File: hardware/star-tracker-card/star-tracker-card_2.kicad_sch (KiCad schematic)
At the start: 94 parts, among them Q2 PMV45EN, Q3 DMP2240UDM, Q4 PMV45EN, Q5 DMP3050LVT-7, Q6 DMP3050LVT-7, U12 MIC842LYC5, U13 MIC842LYC5, U14 MAX4211FETE, U15 TPS62112, U16 MAX7310ATE, U2 TS5A21366DCUR

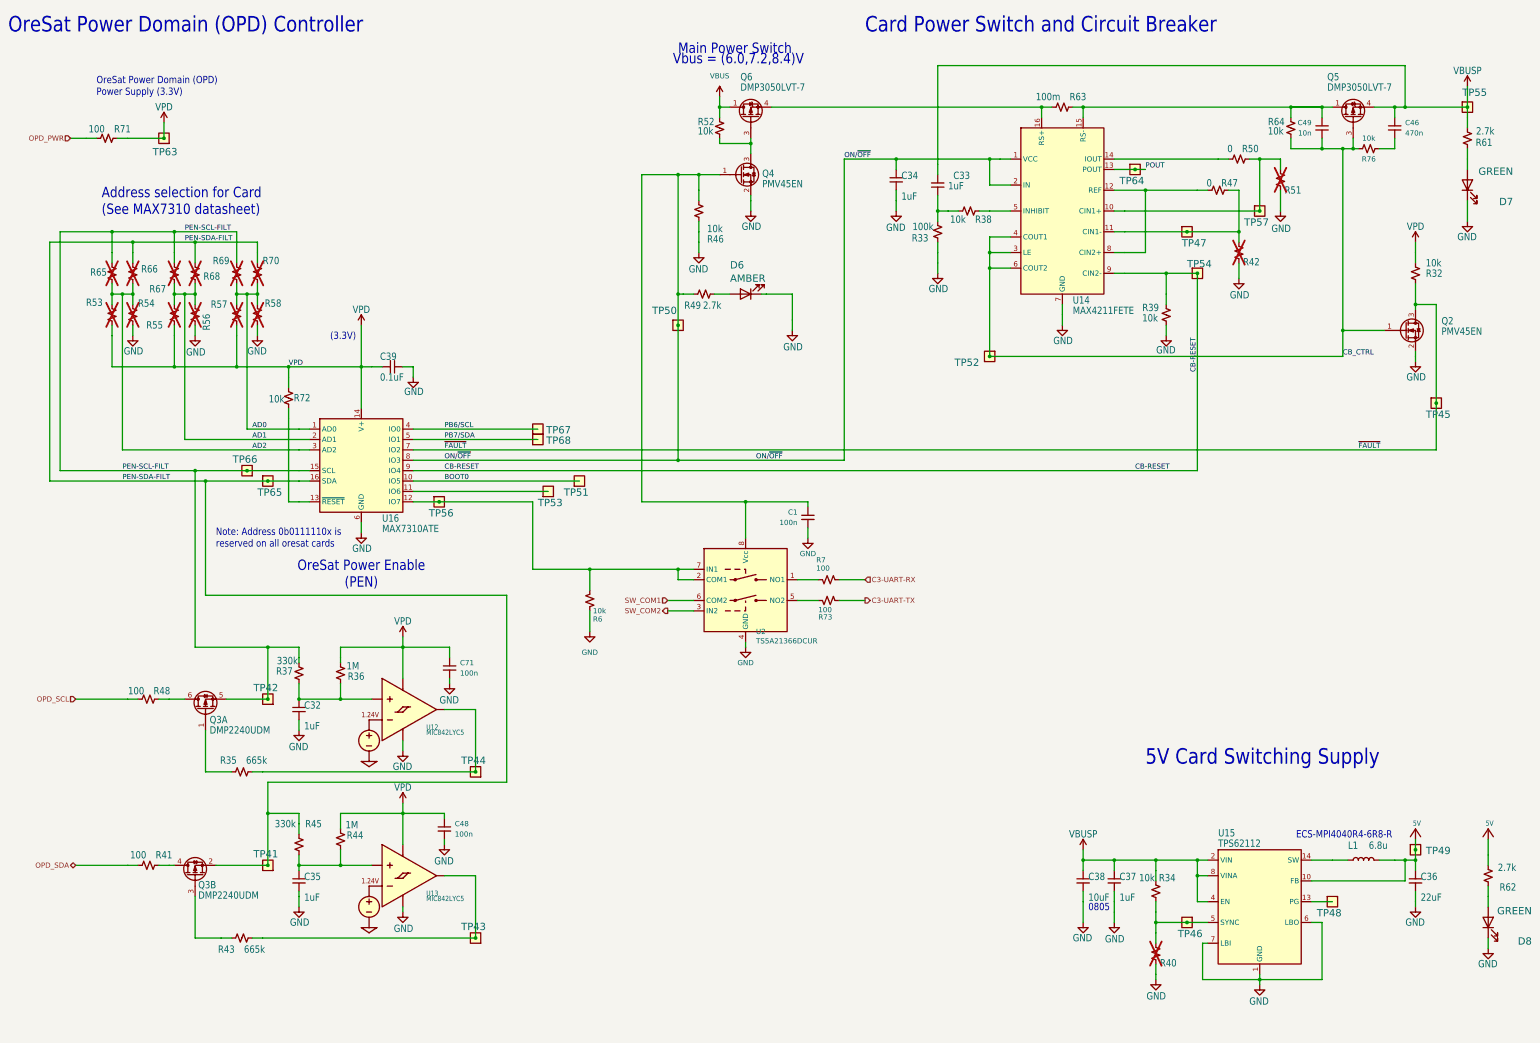
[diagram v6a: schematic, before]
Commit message: Big almost-done cleanup
Fixed a bunch of things in the schematic. Compared against C3 Octavo. Fixed all weird ERCs. Cleaned up a lot of planes on the layout. Moved uart switch, rerouted a bunch of traces for better layout. Fixed library issues, and board/sch sync issues.
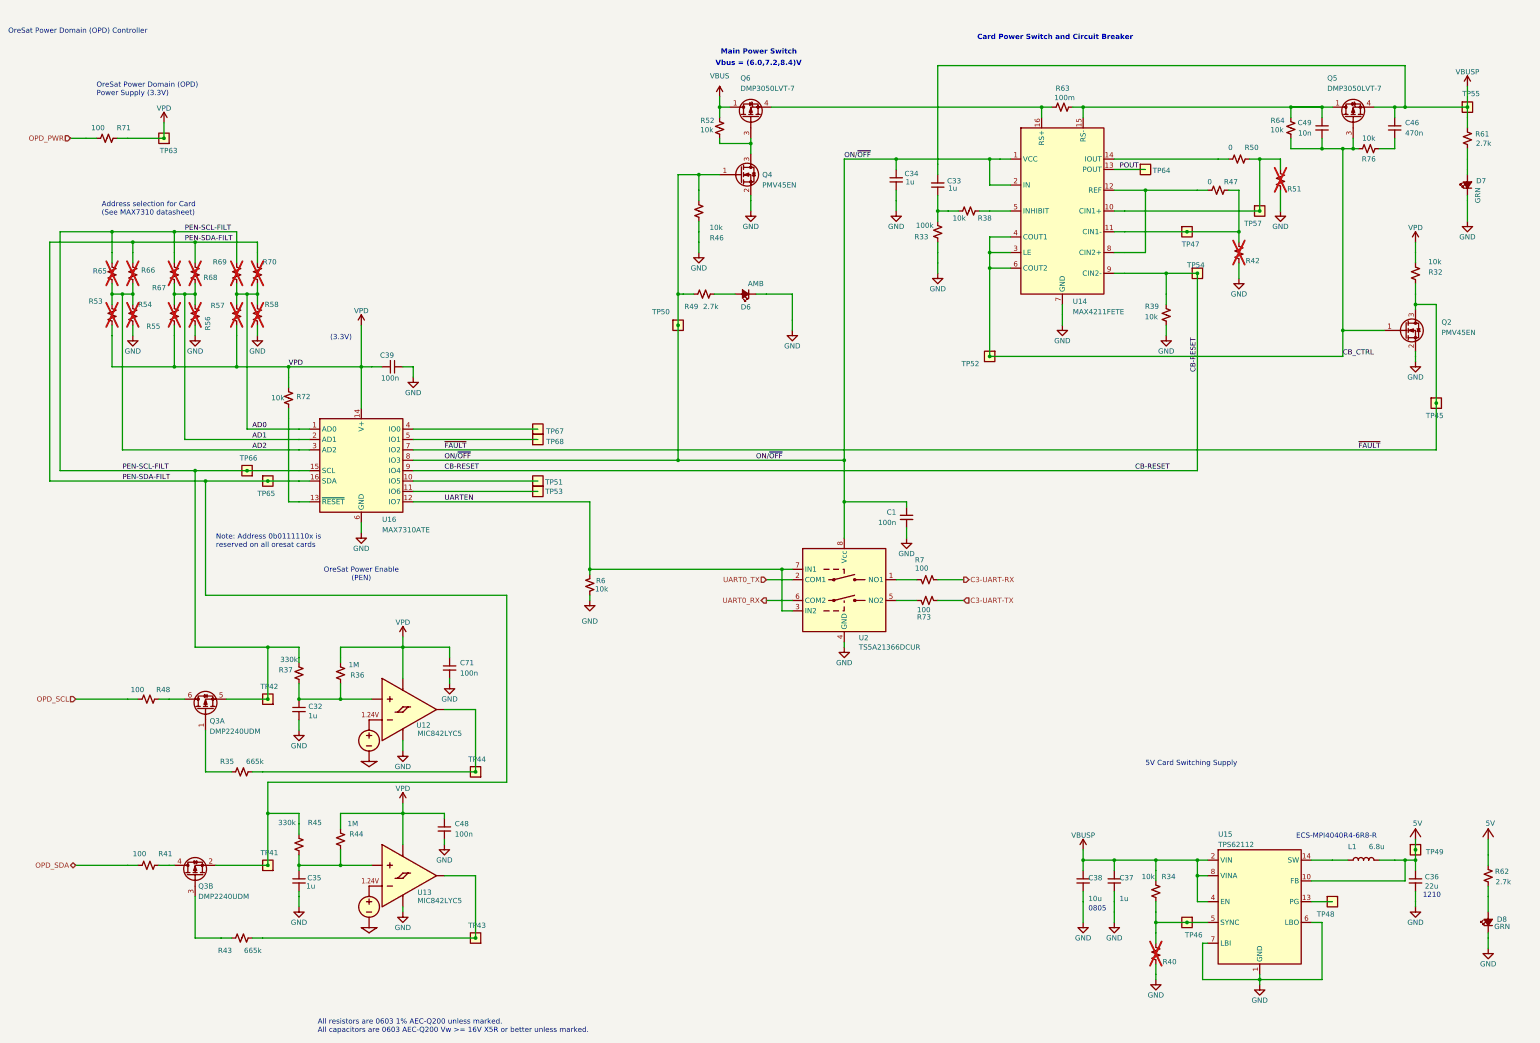
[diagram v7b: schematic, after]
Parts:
- removed TP56: TEST-POINT, star-tracker-card:2MM-TEST-POINT, symbol star-tracker-card-eagle-import:TEST-POINT
- C1, C46: footprint oresat-passives:c_0603-SMALL -> oresat-passives:0603-C-NOSILK
- C32, C35: value 1uF -> 1u; footprint oresat-passives:0805-C-NOSILK -> oresat-passives:0603-C-NOSILK
- C33: value 1uF -> 1u; footprint oresat-passives:c_0603-SMALL -> oresat-passives:0603-C-NOSILK; DIS Digi-Key -> (none); DPN 1276-1001-1-ND -> (none); MFR Samsung -> (none); MPN CL05B104KO5NNNC -> (none)
- C34, C37: value 1uF -> 1u; footprint oresat-passives:c_0603-SMALL -> oresat-passives:0603-C-NOSILK
- C36: value 22uF -> 22u; footprint oresat-passives:0805-B-NOSILK -> Capacitor_SMD:C_1210_3225Metric
- C38: value 10uF -> 10u
- C39: value 0.1uF -> 100n; footprint oresat-passives:c_0603-SMALL -> oresat-passives:0603-C-NOSILK
- C48, C49, C71: DIST DigiKey -> (none)
- D6: value AMBER -> AMB; symbol Device:LED -> Device:LED_Small_Filled
- D7, D8: value GREEN -> GRN; symbol Device:LED -> Device:LED_Small_Filled
- R32, R33, R34, R36, R37, R38, R39, R41, R44, R45, R46, R47, R48, R49, R50, R52, R6, R61, R62, R64, R7, R71, R72, R73: footprint Resistor_SMD:R_0603_1608Metric -> oresat-passives:0603-C-NOSILK
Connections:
- net SW_COM2 is gone; now on net UARTEN: U2.3 (IN2)
- net UARTEN: now reaches R6.2, U16.12 (IO7), U2.7 (IN1)
- net UARTEN: no longer U2.2 (COM1)
- net BOOT0: no longer names the net of TP51.1, U16.10 (IO5)
- net PB6/SCL: no longer names the net of TP67.1, U16.4 (IO0)
- net PB7/SDA: no longer names the net of TP68.1, U16.5 (IO1)
- net SW_COM1 renamed UART0_RX
- new net UART0_TX: U2.2 (COM1)
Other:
- note added: "1210"
- note added: "All resistors are 0603 1% AEC-Q200 unless marked. All capacitors are 0603 AEC-Q200 Vw >= 16V X5R or better unless marked."
- moved on the sheet: C1, R6, R7, R73, TP51, TP53, TP64, U2

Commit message: BOM 99% completed, push for final review
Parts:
- C1, C39: DIS (none) -> DigiKey; DPN (none) -> 399-6856-1-ND; MFR (none) -> KEMET; MPN (none) -> C0603C104K5RACAUTO
- C32, C33, C34, C35, C37: DIS (none) -> DigiKey; DPN (none) -> 490-GRT188R71E105KE13DCT-ND; MFR (none) -> Murata Electronics; MPN (none) -> GRT188R71E105KE13D
- C36: DIS (none) -> DigiKey; DPN (none) -> 587-5949-1-ND; MFR (none) -> Taiyo Yuden; MPN (none) -> TMK325B7226KMHP
- C38: DIS (none) -> DigiKey; DPN (none) -> 490-GRT21BC71E106KE13KCT-ND; MFR (none) -> Murata Electronics; MPN (none) -> GRT21BC71E106KE13K
- C46: DIS (none) -> DigiKey; DPN (none) -> 399-C0603C474K3RACAUTOCT-ND; MFR (none) -> KEMET; MPN (none) -> C0603C474K3RACAUTO
- C48, C49, C71: DIS (none) -> DigiKey
- D6: DIS (none) -> DigiKey; DPN (none) -> 732-150060AS75000CT-ND; MFR (none) -> Wurth; MPN (none) -> 150060AS75000
- D7, D8: DIS (none) -> DigiKey; DPN (none) -> 732-4971-1-ND; MFR (none) -> Wurth; MPN (none) -> 150060GS75000
- L1: DIS (none) -> DigiKey; DPN (none) -> XC2337CT-ND; MFR (none) -> ECS; MPN (none) -> ECS-MPI4040R4-6R8-R
- Q2, Q4: value PMV45EN -> DMN3028LQ-7; DIS (none) -> DigiKey; DPN 1727-2307-1-ND -> 31-DMN3028LQ-7CT-ND; MFR (none) -> Diodes Incorporated; MPN PMV45EN2R -> DMN3028LQ-7
- Q3: DIS (none) -> DigiKey; DPN (none) -> DMP2240UDMDICT-ND; MFR (none) -> Diodes Inc; MPN (none) -> DMP2240UDM-7
- Q5, Q6: DIS (none) -> DigiKey; DPN (none) -> 31-DMP3050LVTQ-7-ND; MFR (none) -> Diodes Inc; MPN DMP3050LVT-7 -> DMP3050LVTQ-7
- R32, R34, R39, R46, R52, R6, R64, R72, R76: DIS (none) -> DigiKey; DPN (none) -> RMCF0603FT10K0CT-ND; MFR (none) -> Stackpole Electronics; MPN (none) -> RMCF0603FT10K0
- R33: DIS Digi-Key -> DigiKey; DPN 1276-4275-1-ND -> RMCF0603FT100KCT-ND; MFR Samsung -> Stackpole Electronics; MPN RC1005F6653CS -> RMCF0603FT100K
- R35, R43: DIS (none) -> DigiKey; DPN (none) -> RMCF0603FT665KCT-ND; MFR (none) -> Stackpole Electronics Inc; MPN (none) -> RMCF0603FT665K
- R36, R44: DIS (none) -> DigiKey; DPN (none) -> RMCF0603FT1M00CT-ND; MFR (none) -> Stackpole Electronics; MPN (none) -> RMCF0603FT1M00
- R37, R45: DIS (none) -> DigiKey; DPN (none) -> RMCF0603FT330KCT-ND; MFR (none) -> Stackpole Electronics; MPN (none) -> RMCF0603FT330K
- R38: DIS Digi-Key -> DigiKey; DPN 1276-4275-1-ND -> RMCF0603FT10K0CT-ND; MFR Samsung -> Stackpole Electronics; MPN RC1005F6653CS -> RMCF0603FT10K0
- R41, R48, R7, R71, R73: DIS (none) -> DigiKey; DPN (none) -> RMCF0603FT100RCT-ND; MFR (none) -> Stackpole Electronics; MPN (none) -> RMCF0603FT100R
- R47, R50: DIS (none) -> DigiKey; DPN (none) -> RMCF0603ZT0R00CT-ND; MFR (none) -> Stackpole Electronics; MPN (none) -> RMCF0603ZT0R00
- R49, R61, R62: DIS (none) -> DigiKey; DPN (none) -> RMCF0603FT2K70CT-ND; MFR (none) -> Stackpole Electronics; MPN (none) -> RMCF0603FT2K70
- R63: DIS (none) -> DigiKey; DPN (none) -> CSR1206FKR100CT-ND; MFR (none) -> Stackpole Electronics; MPN (none) -> CSR1206FKR100
- U12, U13: DIS (none) -> DigiKey; DPN (none) -> 576-2927-1-ND; MFR (none) -> Microchip; MPN (none) -> MIC842LYC5-TR
- U14: DIS (none) -> DigiKey; DPN (none) -> MAX4211FETE+-ND; MFR (none) -> Analog Devices; MPN (none) -> MAX4211FETE
- U15: DIS (none) -> DigiKey; DPN (none) -> 296-39444-1-ND; MFR (none) -> Texas Instruments; MPN (none) -> TPS62112RSAR
